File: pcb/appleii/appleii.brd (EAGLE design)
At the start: 75 x 47 mm, 19 parts, among them J1 POWER_JACKPTH, J2 ATX24RH

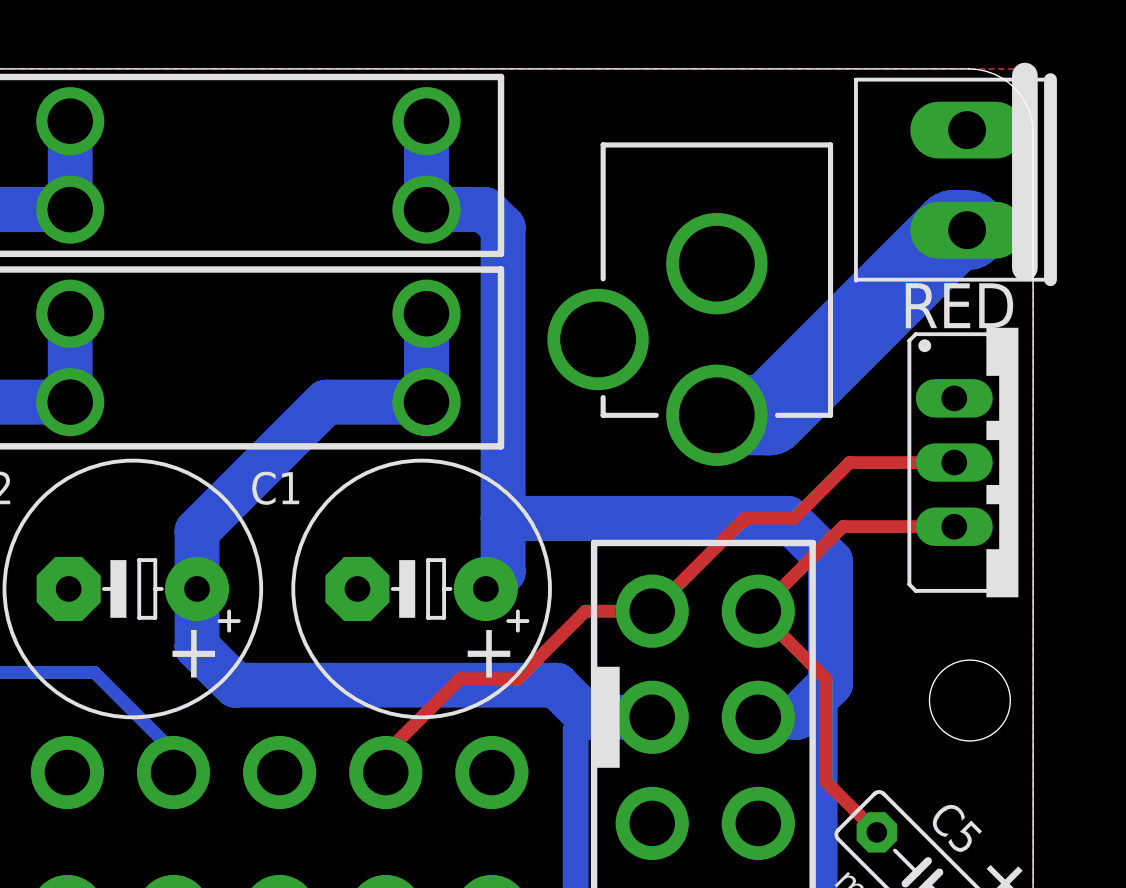
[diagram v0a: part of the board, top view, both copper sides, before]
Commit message: updated silkscreen and switched to terminal block for power input
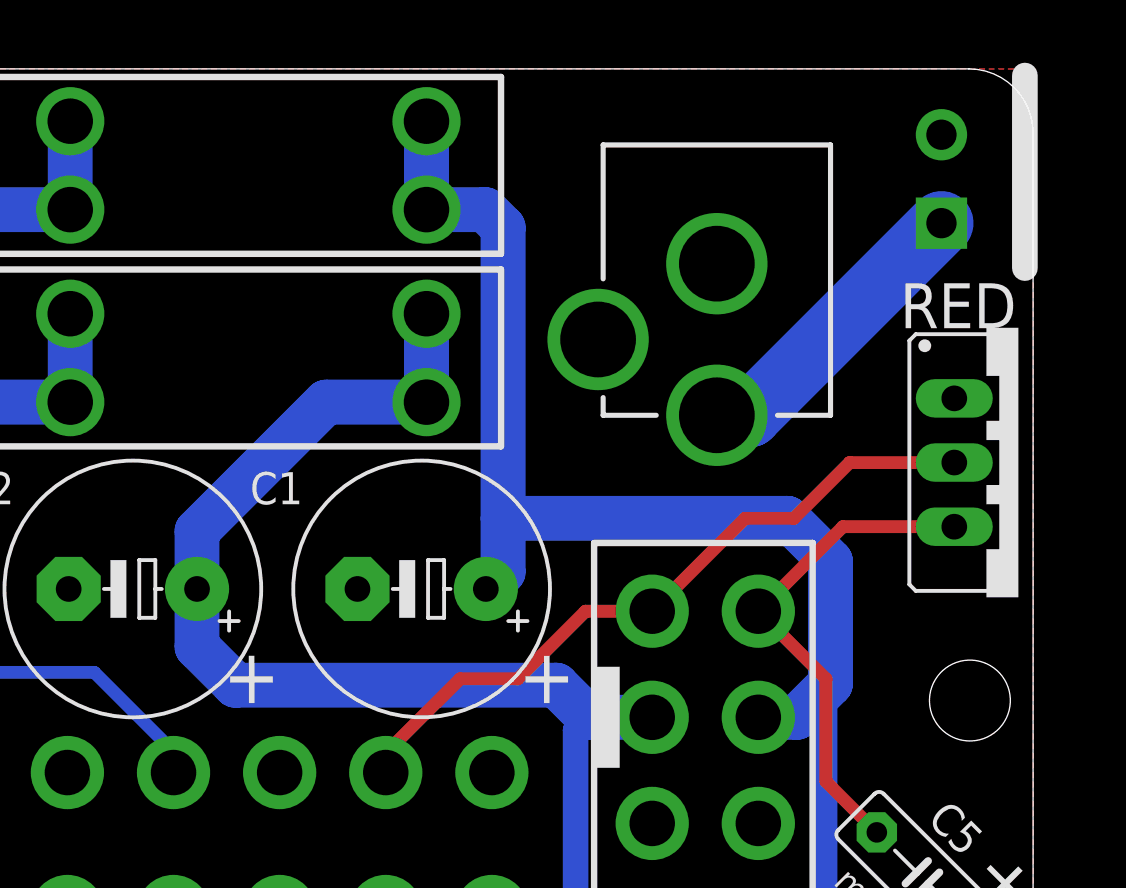
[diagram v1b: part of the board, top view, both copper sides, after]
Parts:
- removed U$7: VH396_2P, 396_conn:396_2P
- added J3: (no value), atx_power_control:SCREWTERMINAL-3.5MM-2-NS
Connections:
- net GND: now also J3.2; no longer U$7.P$1
- net N$1: now also J3.1; no longer U$7.P$2
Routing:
- net N$1: track 12.9 -> 12.0 mm
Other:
- board text added: "12V"
- board text added: "12V Center Positive"
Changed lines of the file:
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@@
 <text x="3.947" y="2.16" size="2.1844" layer="25" distance="35" rot="MR0" align="center">+</text>
 <text x="3.947" y="11.05" size="2.1844" layer="25" distance="35" align="center">+</text>
-<text x="41.783" y="24.003" size="2.1844" layer="25" distance="35" align="center">+</text>
-<text x="53.467" y="24.003" size="2.1844" layer="25" distance="35" align="center">+</text>
+<text x="44.069" y="22.987" size="2.1844" layer="25" distance="35" align="center">+</text>
+<text x="55.753" y="22.987" size="2.1844" layer="25" distance="35" align="center">+</text>
 <wire x1="74.676" y1="46.736" x2="74.676" y2="39.116" width="1.016" layer="21"/>
 <text x="69.216" y="13.325" size="1.016" layer="25" distance="35" rot="R315" align="center">min 1uF</text>
@@
 <text x="9.263" y="41.113" size="1.778" layer="25" rot="R270" align="center">PS_ON</text>
 <text x="9.687" y="34.409" size="1.778" layer="25" align="center">PS_ON</text>
+<text x="60.706" y="44.196" size="1.4224" layer="26" distance="35" rot="MR0" align="center">12V
+Center
+Positive</text>
+<text x="68.485" y="44.4842" size="1.27" layer="26" distance="35" rot="MR0" align="center">GND</text>
+<text x="68.485" y="40.9282" size="1.27" layer="26" distance="35" rot="MR0" align="center">12V</text>
 </plain>
 <attributes>
@@
 <element name="JP4" library="appleii" package="1X04" value="" x="61.468" y="5.842" smashed="yes" rot="R270"/>
 <element name="JP1" library="appleii" package="1X04" value="" x="69.596" y="5.842" smashed="yes" rot="R270"/>
-<element name="U$7" library="396_conn" package="396_2P" value="VH396_2P" x="72.39" y="42.5958" smashed="yes" rot="R270"/>
+<element name="J3" library="atx_power_control" package="SCREWTERMINAL-3.5MM-2-NS" value="" x="71.374" y="40.894" smashed="yes" rot="R90">
+<attribute name="PROD_ID" value="CONN-13512" x="71.374" y="40.894" size="1.778" layer="27" rot="R90" display="off"/>
+<attribute name="SF_ID" value="PRT-09918" x="71.374" y="40.894" size="1.778" layer="27" rot="R90" display="off"/>
+<attribute name="SF_SKU" value="PRT-08432" x="71.374" y="40.894" size="1.778" layer="27" rot="R90" display="off"/>
+<attribute name="SKU" value="PRT-09914" x="71.374" y="40.894" size="1.778" layer="27" rot="R90" display="off"/>
+<attribute name="VALUE" x="70.104" y="39.624" size="0.6096" layer="27" font="vector" ratio="20" rot="R90"/>
+</element>
 </elements>
 <signals>
@@
 <contactref element="J1" pad="GNDBREAK"/>
 <contactref element="J1" pad="GND"/>
-<contactref element="U$7" pad="P$1"/>
+<contactref element="J3" pad="2"/>
 </signal>
 <signal name="+5V">
@@
 <signal name="N$1">
 <contactref element="J1" pad="PWR"/>
-<contactref element="U$7" pad="P$2"/>
-<wire x1="62.484" y1="33.29" x2="64.532" y2="33.29" width="3.175" layer="16"/>
-<wire x1="71.8578" y1="40.6158" x2="72.39" y2="40.6158" width="3.175" layer="16"/>
-<wire x1="64.532" y1="33.29" x2="71.8578" y2="40.6158" width="3.175" layer="16"/>
+<contactref element="J3" pad="1"/>
+<wire x1="71.374" y1="40.894" x2="63.77" y2="33.29" width="2.54" layer="16"/>
+<wire x1="63.77" y1="33.29" x2="62.484" y2="33.29" width="2.54" layer="16"/>
 </signal>
 </signals>
